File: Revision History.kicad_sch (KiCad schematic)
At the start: 0 parts

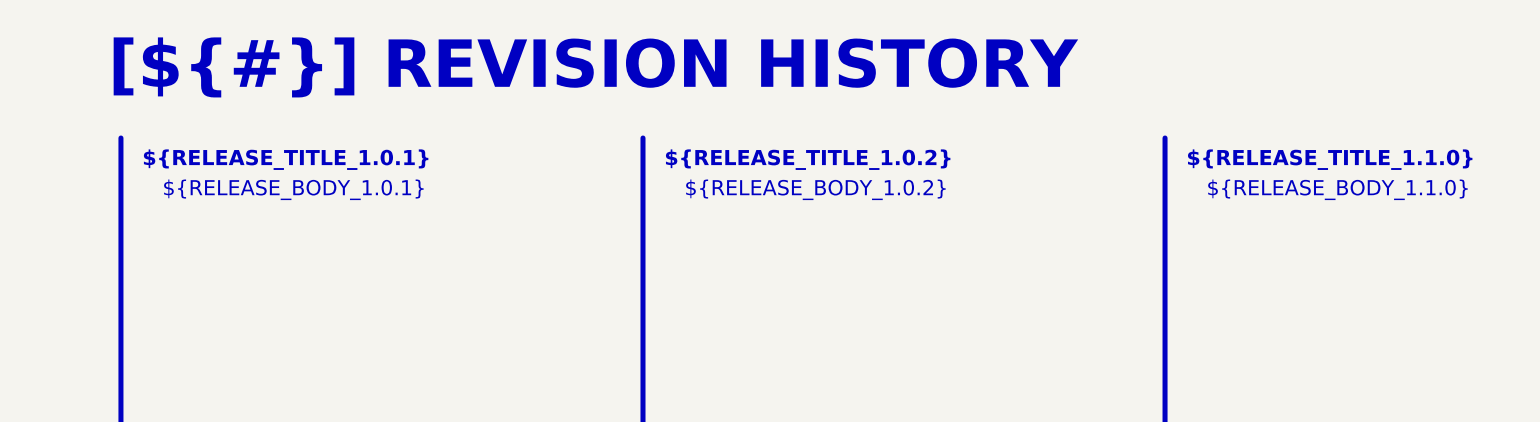
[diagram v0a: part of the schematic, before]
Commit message: fix: change status led wiring and improve 12V input protection
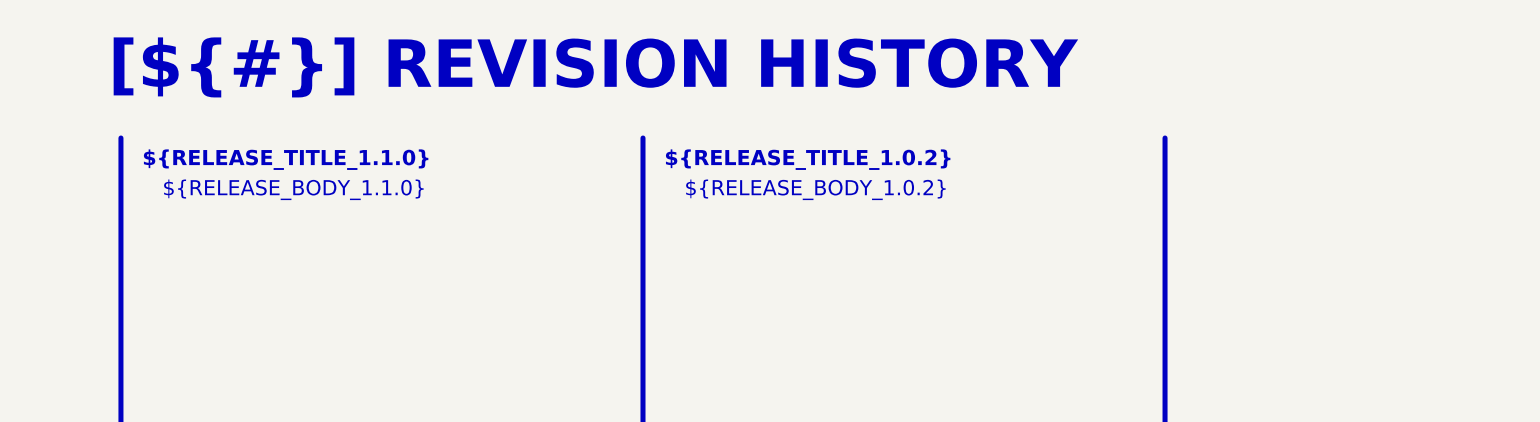
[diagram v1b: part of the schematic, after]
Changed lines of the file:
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@@
 		(company "${COMPANY}")
-	)
-	(text_box "${RELEASE_BODY_1.1.0}"
-		(exclude_from_sim no)
-		(at 224.79 35.56 0)
-		(size 58.42 97.79)
-		(margins 1.4287 1.4287 1.4287 1.4287)
-		(stroke
-			(width -0.0001)
-			(type default)
-		)
-		(fill
-			(type none)
-		)
-		(effects
-			(font
-				(face "Arial")
-				(size 1.905 1.905)
-				(color 0 0 0 1)
-			)
-			(justify left top)
-		)
 	)
 	(text_box "[${#}] ${TITLE}"
@@
 		)
 	)
-	(text_box "${RELEASE_BODY_1.0.1}"
+	(text_box "${RELEASE_BODY_1.1.0}"
 		(exclude_from_sim no)
 		(at 92.71 35.56 0)
@@
 		)
 	)
-	(text_box "${RELEASE_TITLE_1.0.1}"
+	(text_box "${RELEASE_TITLE_1.1.0}"
 		(exclude_from_sim no)
 		(at 90.17 31.75 0)
 		(size 57.15 7.62)
 		(margins 1.4287 1.4287 1.4287 1.4287)
-		(stroke
-			(width -0.0001)
-			(type default)
-		)
-		(fill
-			(type none)
-		)
-		(effects
-			(font
-				(face "Arial")
-				(size 1.905 1.905)
-				(thickness 0.254)
-				(bold yes)
-			)
-			(justify left top)
-		)
-	)
-	(text_box "${RELEASE_TITLE_1.1.0}"
-		(exclude_from_sim no)
-		(at 222.25 31.75 0)
-		(size 57.15 7.62)
-		(margins 1.4287 1.4287 1.4287 1.4287)
